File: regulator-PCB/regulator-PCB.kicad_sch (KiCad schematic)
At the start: 10 parts, among them J1 Conn_ARM_SWD_TagConnect_TC2030, J2 PJ-059A, U1 STM32C092KCT6, U2 LP2985-3.3

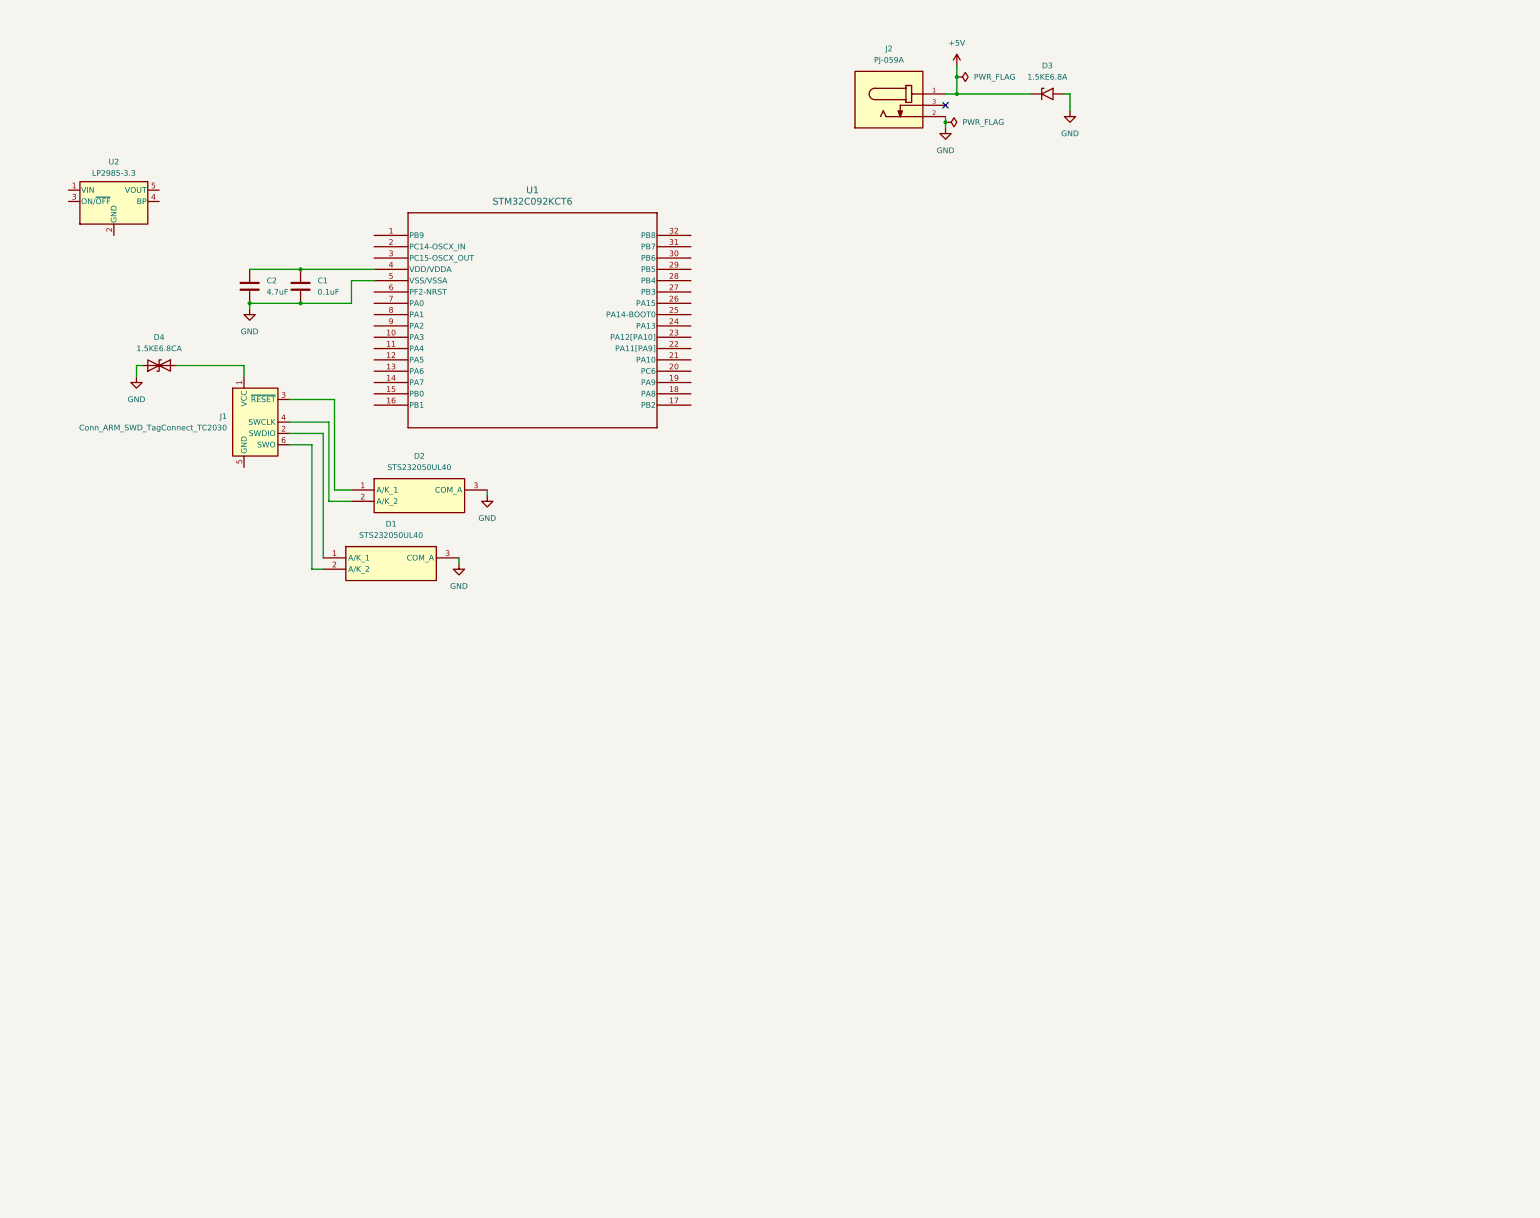
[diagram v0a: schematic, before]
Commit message: initial schematic for regulator PCB
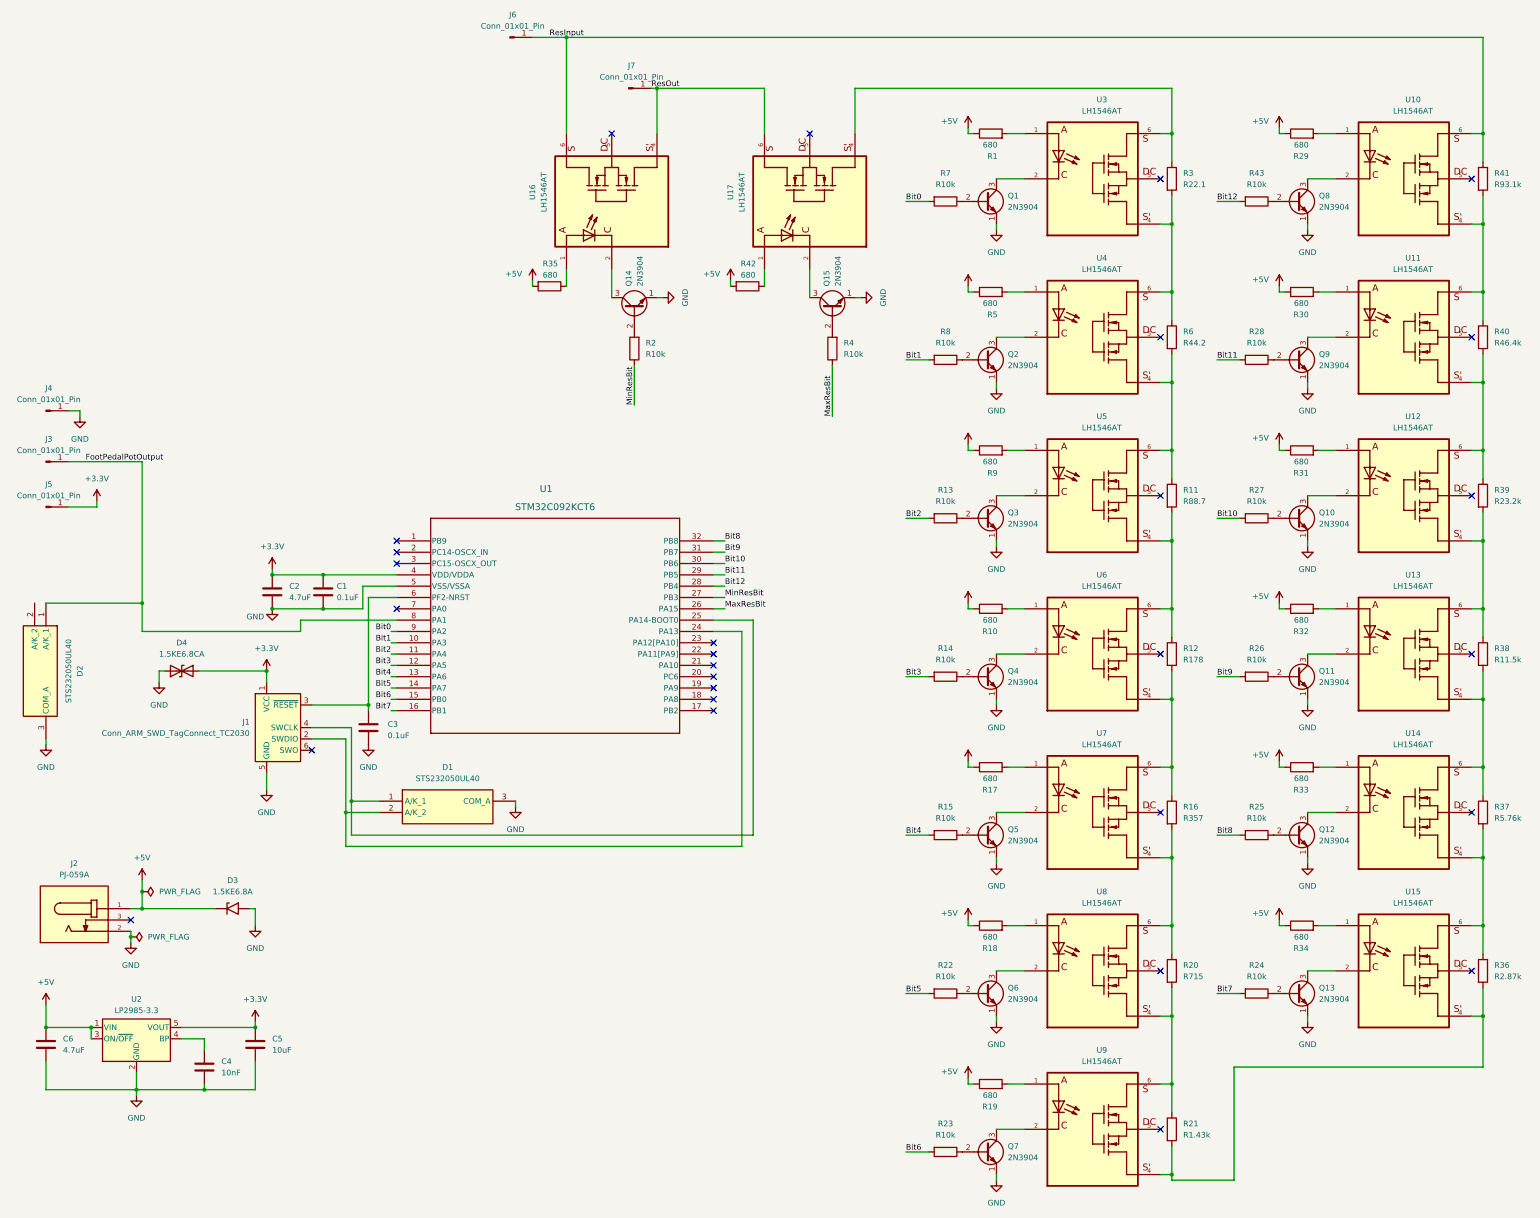
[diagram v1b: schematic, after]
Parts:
- added C3: 0.1uF, project:CAP_C320_KEM, symbol regulator-PCB:C320C104K5R5TA
- added C4: 10nF, Capacitor_THT:C_Rect_L13.0mm_W4.0mm_P10.00mm_FKS3_FKP3_MKS4, symbol regulator-PCB:B32621A6103J189
- added C5: 10uF, Capacitor_THT:CP_Radial_Tantal_D5.5mm_P5.00mm, symbol regulator-PCB:FG20X7R1H106KRT06
- added C6: 4.7uF, project:CAPRB500W50L450T300H550, symbol regulator-PCB:FG24X7R1E475KRT00
- added J3, J4, J5, J6, J7: Conn_01x01_Pin, Connector_Wire:SolderWire-0.5sqmm_1x01_D0.9mm_OD2.3mm_Relief2x, symbol Connector:Conn_01x01_Pin
- added Q1, Q10, Q11, Q12, Q13, Q14, Q15, Q2, Q3, Q4, Q5, Q6, Q7, Q8, Q9: 2N3904, Package_TO_SOT_THT:TO-92_Inline, symbol Transistor_BJT:2N3904
- added R1, R10, R17, R18, R19, R29, R30, R31, R32, R33, R34, R35, R42, R5, R9: 680, Resistor_THT:R_Axial_DIN0207_L6.3mm_D2.5mm_P10.16mm_Horizontal, symbol regulator-PCB:R680
- added R11: R88.7, Resistor_THT:R_Axial_DIN0207_L6.3mm_D2.5mm_P10.16mm_Horizontal, symbol regulator-PCB:R88.7
- added R12: R178, Resistor_THT:R_Axial_DIN0207_L6.3mm_D2.5mm_P10.16mm_Horizontal, symbol regulator-PCB:R178
- added R13, R14, R15, R2, R22, R23, R24, R25, R26, R27, R28, R4, R43, R7, R8: R10k, Resistor_THT:R_Axial_DIN0207_L6.3mm_D2.5mm_P10.16mm_Horizontal, symbol regulator-PCB:R10k
- added R16: R357, Resistor_THT:R_Axial_DIN0207_L6.3mm_D2.5mm_P10.16mm_Horizontal, symbol regulator-PCB:R357
- added R20: R715, Resistor_THT:R_Axial_DIN0207_L6.3mm_D2.5mm_P10.16mm_Horizontal, symbol regulator-PCB:R715
- added R21: R1.43k, Resistor_THT:R_Axial_DIN0207_L6.3mm_D2.5mm_P10.16mm_Horizontal, symbol regulator-PCB:R1.43k
- added R3: R22.1, Resistor_THT:R_Axial_DIN0207_L6.3mm_D2.5mm_P10.16mm_Horizontal, symbol regulator-PCB:R22.1
- added R36: R2.87k, Resistor_THT:R_Axial_DIN0207_L6.3mm_D2.5mm_P10.16mm_Horizontal, symbol regulator-PCB:R2.87k
- added R37: R5.76k, Resistor_THT:R_Axial_DIN0207_L6.3mm_D2.5mm_P10.16mm_Horizontal, symbol regulator-PCB:R5.76k
- added R38: R11.5k, Resistor_THT:R_Axial_DIN0207_L6.3mm_D2.5mm_P10.16mm_Horizontal, symbol regulator-PCB:R11.5k
- added R39: R23.2k, Resistor_THT:R_Axial_DIN0207_L6.3mm_D2.5mm_P10.16mm_Horizontal, symbol regulator-PCB:R23.2k
- added R40: R46.4k, Resistor_THT:R_Axial_DIN0207_L6.3mm_D2.5mm_P10.16mm_Horizontal, symbol regulator-PCB:R46.4k
- added R41: R93.1k, Resistor_THT:R_Axial_DIN0207_L6.3mm_D2.5mm_P10.16mm_Horizontal, symbol regulator-PCB:R93.1k
- added R6: R44.2, Resistor_THT:R_Axial_DIN0207_L6.3mm_D2.5mm_P10.16mm_Horizontal, symbol regulator-PCB:R44.2
- added U10, U11, U12, U13, U14, U15, U16, U17, U3, U4, U5, U6, U7, U8, U9: LH1546AT, project:DIP762W50P254L730H410Q6, symbol regulator-PCB:LH1546AT
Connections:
- net +5V: now also U2.1 (VIN), U2.3 (ON/~{OFF}), C6.1, R1.1, R10.1, R17.1, R18.1, R19.1, R29.1, R30.1, R31.1, R32.1, R33.1, R34.1, R35.2, R42.2, R5.1, R9.1
- net GND: now also J1.5 (GND), U2.2 (GND), C3.2, C4.2, C5.2, C6.2, J4.1 (Pin_1), Q1.1 (E), Q10.1 (E), Q11.1 (E), Q12.1 (E), Q13.1 (E), Q14.1 (E), Q15.1 (E), Q2.1 (E), Q3.1 (E), Q4.1 (E), Q5.1 (E), Q6.1 (E), Q7.1 (E), Q8.1 (E), Q9.1 (E)
- net at J1.3 (~{RESET}): now also U1.6 (PF2-NRST), C3.1; no longer D2.1 (A/K_1)
- net at J1.4 (SWCLK): now also D1.1 (A/K_1), U1.25 (PA14-BOOT0); no longer D2.2 (A/K_2)
- net +3.3V: now reaches D4.2 (A2), J1.1 (VCC)
- net +3.3V: now also C1.1, C2.1, U1.4 (VDD/VDDA), U2.5 (VOUT), C5.1, J5.1 (Pin_1)
- net at J1.2 (SWDIO): now also D1.2 (A/K_2), U1.24 (PA13); no longer D1.1 (A/K_1)
- net at J1.6 (SWO): no longer D1.2 (A/K_2)
- net at U2.4 (BP): now also C4.1
- net Bit1: now reaches U1.10 (PA3)
- net Bit1: now also R8.2
- net Bit2: now reaches U1.11 (PA4)
- net Bit2: now also R13.2
- net Bit3: now reaches U1.12 (PA5)
- net Bit3: now also R14.2
- net Bit4: now reaches U1.13 (PA6)
- net Bit4: now also R15.2
- net Bit5: now reaches U1.14 (PA7)
- net Bit5: now also R22.2
- net Bit6: now reaches U1.15 (PB0)
- net Bit6: now also R23.2
- net Bit7: now reaches U1.16 (PB1)
- net Bit7: now also R24.2
- net MaxResBit: now reaches U1.26 (PA15)
- net MaxResBit: now also R4.1
- net MinResBit: now reaches U1.27 (PB3)
- net MinResBit: now also R2.1
- net Bit12: now reaches U1.28 (PB4)
- net Bit12: now also R43.2
- net Bit11: now reaches U1.29 (PB5)
- net Bit11: now also R28.2
- net Bit10: now reaches U1.30 (PB6)
- net Bit10: now also R27.2
- net Bit9: now reaches U1.31 (PB7)
- net Bit9: now also R26.2
- net Bit8: now reaches U1.32 (PB8)
- net Bit8: now also R25.2
- net FootPedalPotOutput: now reaches U1.8 (PA1)
- net FootPedalPotOutput: now also D2.1 (A/K_1), J3.1 (Pin_1)
- net Bit0: now reaches U1.9 (PA2)
- net Bit0: now also R7.2
- new net: R30.2, U11.1
- new net: R36.1, R37.2, U14.4, U15.6
- new net: R21.2, R36.2, U15.4, U9.4
- new net: R31.2, U12.1
- new net: Q10.3 (C), U12.2
- new net: R38.1, R39.2, U12.4, U13.6
- new net: R39.1, R40.2, U11.4, U12.6
- new net: Q11.2 (B), R26.1
- new net: R19.2, U9.1
- new net: Q7.3 (C), U9.2
- new net: R20.2, R21.1, U8.4, U9.6
- new net: R34.2, U15.1
- new net: Q14.2 (B), R2.2
- new net: Q14.3 (C), U16.2
- new net: R11.1, R6.2, U4.4, U5.6
- new net: R11.2, R12.1, U5.4, U6.6
- new net: R18.2, U8.1
- new net: Q6.3 (C), U8.2
- new net: R16.2, R20.1, U7.4, U8.6
- new net: Q11.3 (C), U13.2
- new net: R17.2, U7.1
- new net: Q7.2 (B), R23.1
- new net: Q12.2 (B), R25.1
- new net: R29.2, U10.1
- new net: Q8.3 (C), U10.2
- new net: R40.1, R41.2, U10.4, U11.6
- new net: R35.1, U16.1
- new net: Q9.2 (B), R28.1
- new net: Q9.3 (C), U11.2
- new net: Q15.2 (B), R4.2
- new net: Q15.3 (C), U17.2
- new net: Q2.2 (B), R8.1
- new net: Q2.3 (C), U4.2
- new net: R12.2, R16.1, U6.4, U7.6
- new net: Q12.3 (C), U14.2
- new net: Q1.2 (B), R7.1
- new net: Q1.3 (C), U3.2
- new net: Q10.2 (B), R27.1
- new net: R5.2, U4.1
- new net: Q8.2 (B), R43.1
- new net: R33.2, U14.1
- new net: R42.1, U17.1
- new net: R3.1, U17.4, U3.6
- new net: R3.2, R6.1, U3.4, U4.6
- new net: R9.2, U5.1
- new net: Q3.3 (C), U5.2
- new net: Q6.2 (B), R22.1
- new net: R37.1, R38.2, U13.4, U14.6
- new net: R32.2, U13.1
- new net: R1.2, U3.1
- new net: Q5.2 (B), R15.1
- new net: Q5.3 (C), U7.2
- new net: R10.2, U6.1
- new net: Q4.2 (B), R14.1
- new net: Q4.3 (C), U6.2
- new net: Q3.2 (B), R13.1
- new net: Q13.2 (B), R24.1
- new net: Q13.3 (C), U15.2
- new net ResInput: J6.1 (Pin_1), R41.1, U10.6, U16.6
- new net ResOut: J7.1 (Pin_1), U16.4, U17.6
- no-connect marks 1 -> 28
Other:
- moved on the sheet: C1, C2, D1, D3, D4, J1, J2, U1, U2

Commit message: ordered JST VH and made speed sensor PCB design
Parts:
- added J10, J8, J9: Conn_01x01_Pin, Connector_Wire:SolderWire-0.5sqmm_1x01_D0.9mm_OD2.3mm_Relief2x, symbol Connector:Conn_01x01_Pin
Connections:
- net +3.3V: now also J10.1 (Pin_1)
- net GND: now also J8.1 (Pin_1)
- net rotary-encoder-output: now reaches U1.18 (PA8)
- net rotary-encoder-output: now also D2.2 (A/K_2), J9.1 (Pin_1)
- no-connect marks 28 -> 27
